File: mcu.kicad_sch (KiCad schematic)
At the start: 30 parts, among them J201 TC2030, U201 nRF54LV10A-CAAA, U202 SiP32431DR3, U203 93AAxxAT-xOT, Y201 Crystal

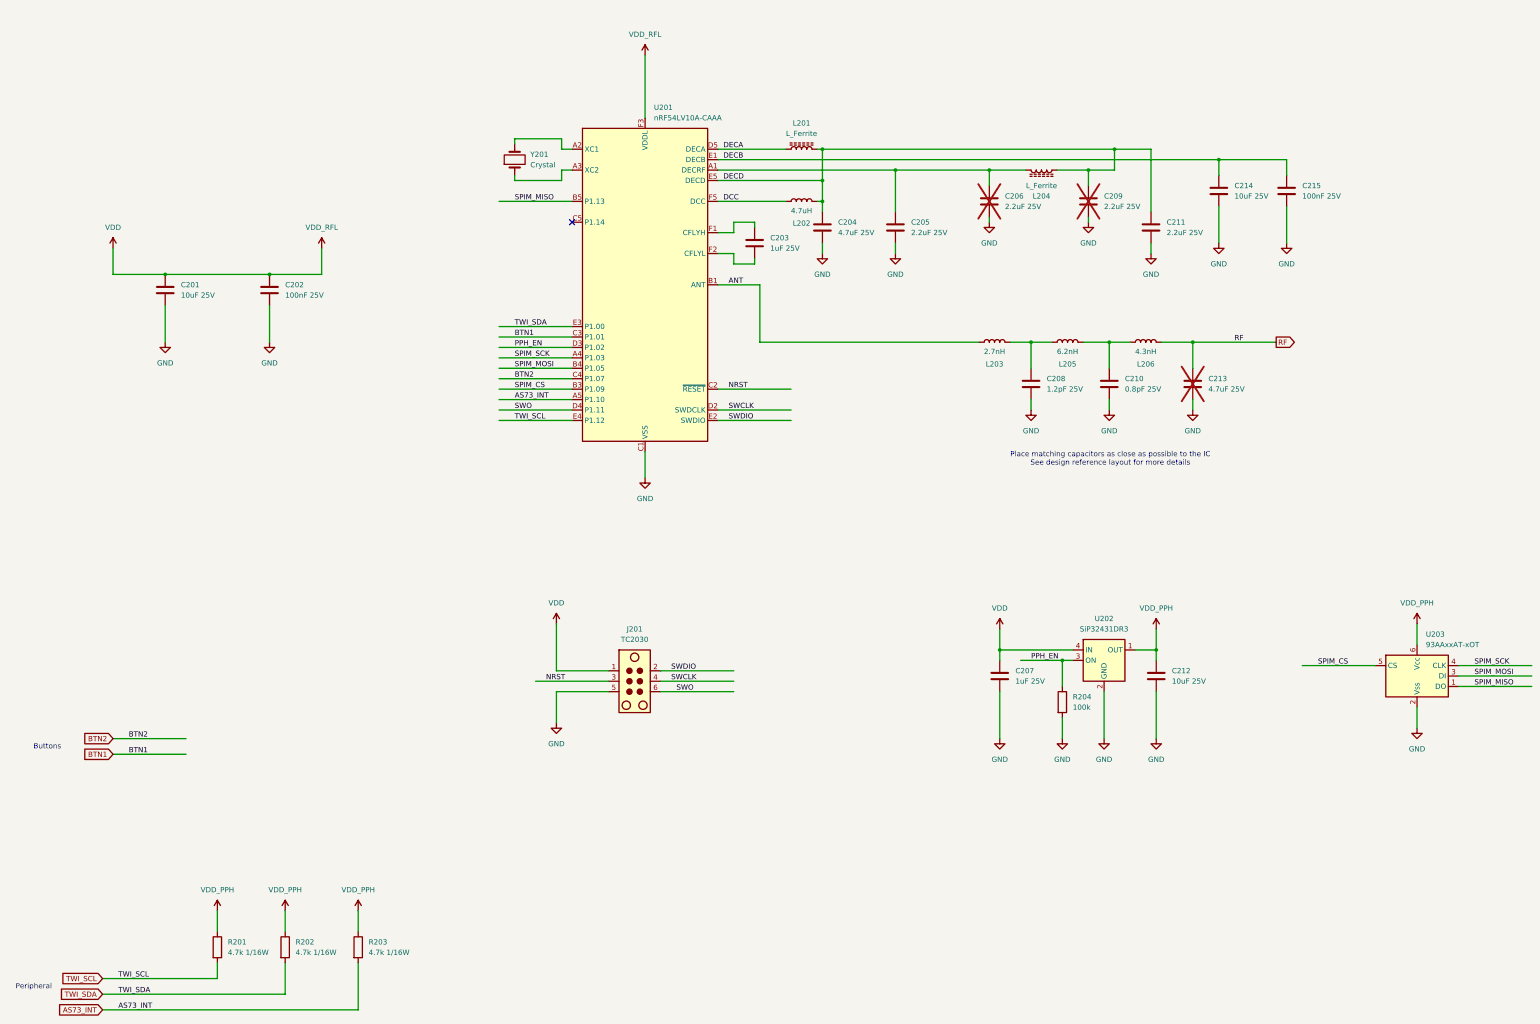
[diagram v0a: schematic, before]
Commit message: Update Schematics - Add footprint to symbols.
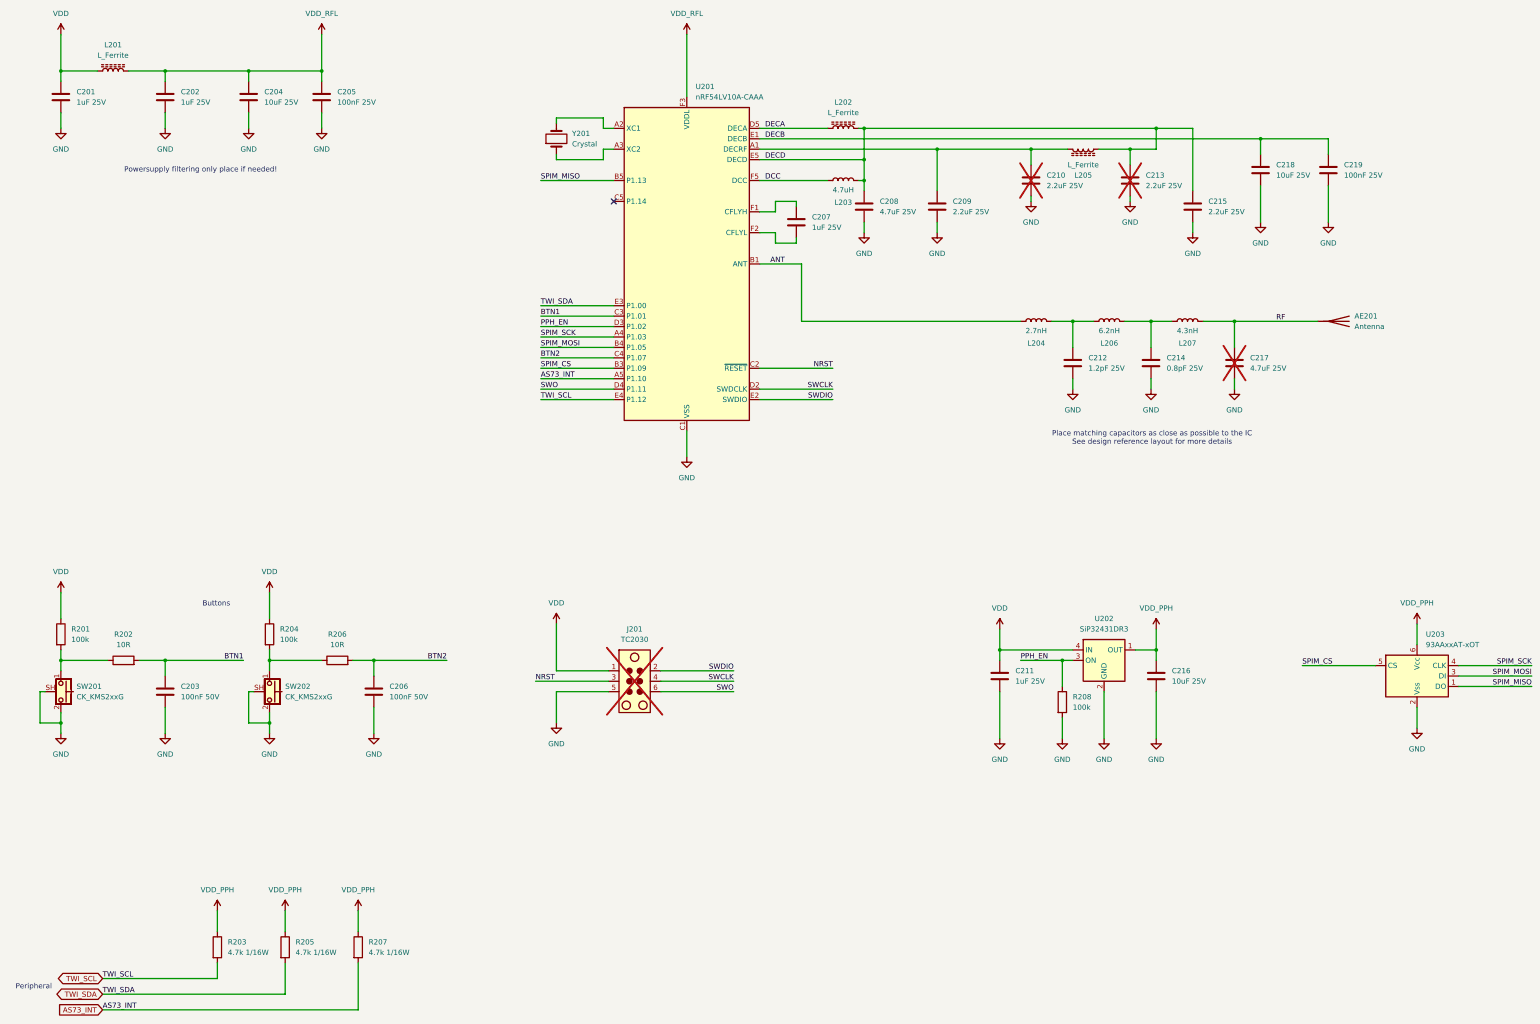
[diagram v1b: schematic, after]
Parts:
- added AE201: Antenna, RF_Antenna:Texas_SWRA117D_2.4GHz_Left, symbol Device:Antenna
- added C201, C202: 1uF 25V, Capacitor_SMD:C_0603_1608Metric, symbol Device:C
- added C203, C206: 100nF 50V, Capacitor_SMD:C_0402_1005Metric, symbol Device:C
- added L201: L_Ferrite, Inductor_SMD:L_0402_1005Metric, symbol Device:L_Ferrite
- added R201, R204: 100k, Resistor_SMD:R_01005_0402Metric, symbol Device:R
- added R202, R206: 10R, Resistor_SMD:R_01005_0402Metric, symbol Device:R
- added SW201, SW202: CK_KMS2xxG, Button_Switch_SMD:SW_SPST_CK_KMS2xxGP, symbol Switch:CK_KMS2xxG
- C204: renamed from C201; footprint (none) -> Capacitor_SMD:C_0603_1608Metric
- C205: renamed from C202; footprint (none) -> Capacitor_SMD:C_0402_1005Metric
- C207: renamed from C203; footprint (none) -> Capacitor_SMD:C_0603_1608Metric
- C208: renamed from C204; footprint (none) -> Capacitor_SMD:C_0603_1608Metric
- C209: renamed from C205; footprint (none) -> Capacitor_SMD:C_0402_1005Metric
- C210: renamed from C206; footprint (none) -> Capacitor_SMD:C_0402_1005Metric
- C211: renamed from C207; footprint (none) -> Capacitor_SMD:C_0402_1005Metric
- C212: renamed from C208; footprint (none) -> Capacitor_SMD:C_0402_1005Metric
- C213: renamed from C209; footprint (none) -> Capacitor_SMD:C_0402_1005Metric
- C214: renamed from C210; footprint (none) -> Capacitor_SMD:C_0402_1005Metric
- C215: renamed from C211; footprint (none) -> Capacitor_SMD:C_0402_1005Metric
- C216: renamed from C212; footprint (none) -> Capacitor_SMD:C_0603_1608Metric
- C217: renamed from C213; footprint (none) -> Capacitor_SMD:C_0603_1608Metric
- C218: renamed from C214; footprint (none) -> Capacitor_SMD:C_0603_1608Metric
- C219: renamed from C215; footprint (none) -> Capacitor_SMD:C_0402_1005Metric
- J201: now not fitted
- L202: renamed from L201; footprint (none) -> Inductor_SMD:L_0402_1005Metric
- L204: renamed from L203; footprint (none) -> Inductor_SMD:L_0402_1005Metric
- L205: renamed from L204; footprint (none) -> Inductor_SMD:L_0402_1005Metric
- L206: renamed from L205; footprint (none) -> Inductor_SMD:L_0402_1005Metric
- L207: renamed from L206; footprint (none) -> Inductor_SMD:L_0402_1005Metric
- R203: renamed from R201; footprint (none) -> Resistor_SMD:R_01005_0402Metric
- R205: renamed from R202; footprint (none) -> Resistor_SMD:R_01005_0402Metric
- R207: renamed from R203; footprint (none) -> Resistor_SMD:R_01005_0402Metric
- R208: renamed from R204; footprint (none) -> Resistor_SMD:R_01005_0402Metric
- Y201: footprint (none) -> Crystal:Crystal_SMD_0603-2Pin_6.0x3.5mm_HandSoldering
- renumbered L202 to L203
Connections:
- net BTN1: now also C203.1, R202.2
- net BTN2: now also C206.1, R206.2
- net GND: now also C201.2, C202.2, C203.2, C206.2, SW201.2, SW201.SH (B), SW202.2, SW202.SH (B)
- net RF: now also AE201.1 (A)
- net VDD: now also C201.1, L201.1, R201.1, R204.1; no longer C204.1, C205.1, U201.F3 (VDDL)
- new net: R204.2, R206.1, SW202.1
- new net: R201.2, R202.1, SW201.1
- new net VDD_RFL: C202.1, C204.1, C205.1, L201.2, U201.F3 (VDDL)
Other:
- note added: "Powersupply filtering only place if needed!"
- moved on the sheet: C204, C205, C207, C208, C209, C210, C212, C213, C214, C215, C217, C218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
